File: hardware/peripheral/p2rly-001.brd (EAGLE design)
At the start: 18 x 31 mm, 4 parts, among them J4 RLY

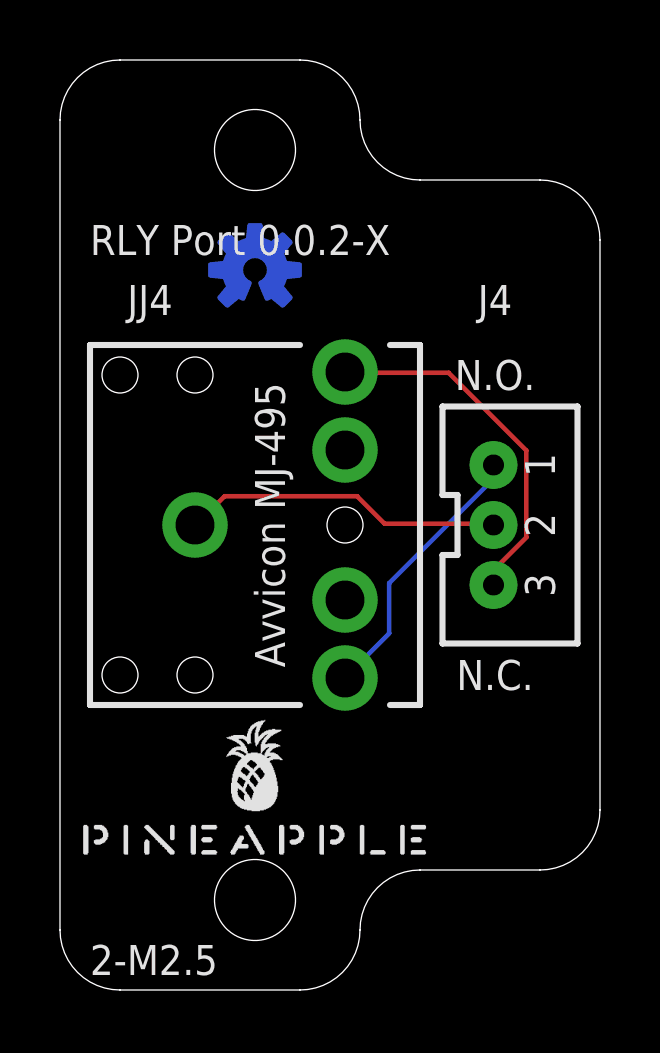
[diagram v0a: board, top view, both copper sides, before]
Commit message: Fixed polarity.
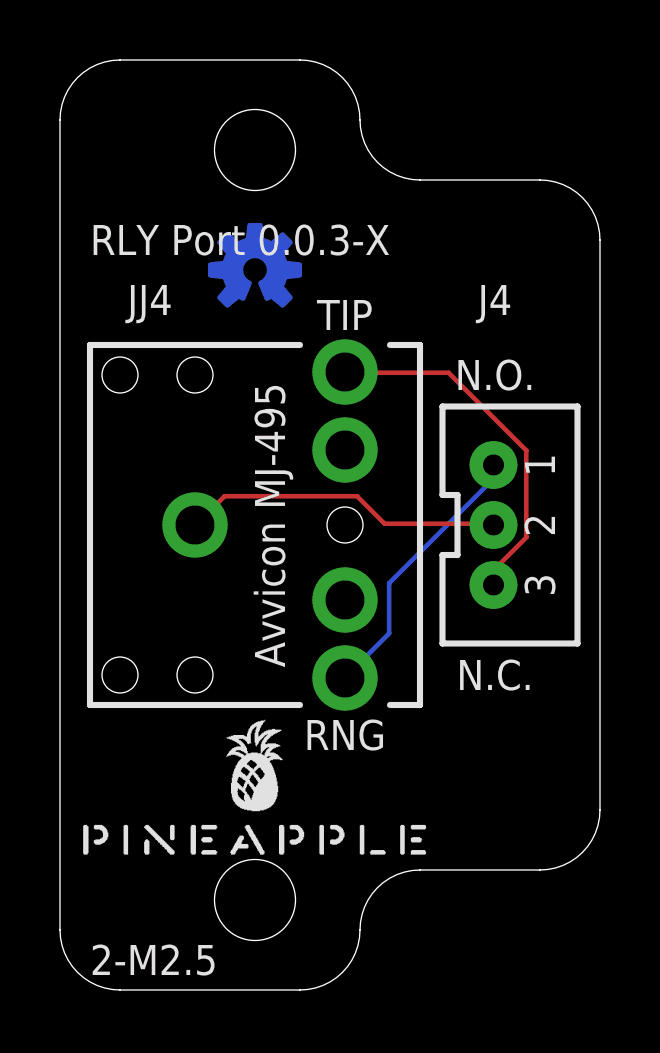
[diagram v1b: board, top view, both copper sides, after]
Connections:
- net NC: now also J4.1, JJ4.TIP; no longer J4.3, JJ4.RING
- net NO: now also J4.3, JJ4.RING; no longer J4.1, JJ4.TIP
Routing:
- net NO: track 9.15 -> 12.1 mm
- net NC: track 12.1 -> 9.15 mm
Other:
- board text added: "RLY Port 0.0.3-X"
- board text added: "RNG"
- board text added: "TIP"
- board text removed: "RLY Port 0.0.2-X"
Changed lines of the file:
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@@
 <grid distance="0.5" unitdist="mm" unit="mm" style="lines" multiple="2" display="yes" altdistance="5" altunitdist="mil" altunit="mil"/>
 <layers>
-<layer number="1" name="Top" color="4" fill="1" visible="no" active="yes"/>
-<layer number="16" name="Bottom" color="1" fill="1" visible="no" active="yes"/>
+<layer number="1" name="Top" color="4" fill="1" visible="yes" active="yes"/>
+<layer number="16" name="Bottom" color="1" fill="1" visible="yes" active="yes"/>
 <layer number="17" name="Pads" color="2" fill="1" visible="yes" active="yes"/>
 <layer number="18" name="Vias" color="2" fill="1" visible="yes" active="yes"/>
 <layer number="19" name="Unrouted" color="6" fill="1" visible="yes" active="yes"/>
 <layer number="20" name="Dimension" color="24" fill="1" visible="yes" active="yes"/>
-<layer number="21" name="tPlace" color="7" fill="1" visible="no" active="yes"/>
-<layer number="22" name="bPlace" color="7" fill="1" visible="yes" active="yes"/>
+<layer number="21" name="tPlace" color="7" fill="1" visible="yes" active="yes"/>
+<layer number="22" name="bPlace" color="7" fill="1" visible="no" active="yes"/>
 <layer number="23" name="tOrigins" color="15" fill="1" visible="yes" active="yes"/>
 <layer number="24" name="bOrigins" color="15" fill="1" visible="no" active="yes"/>
-<layer number="25" name="tNames" color="7" fill="1" visible="no" active="yes"/>
-<layer number="26" name="bNames" color="7" fill="1" visible="yes" active="yes"/>
+<layer number="25" name="tNames" color="7" fill="1" visible="yes" active="yes"/>
+<layer number="26" name="bNames" color="7" fill="1" visible="no" active="yes"/>
 <layer number="27" name="tValues" color="7" fill="1" visible="no" active="yes"/>
 <layer number="28" name="bValues" color="7" fill="1" visible="no" active="yes"/>
@@
 <rectangle x1="9" y1="0" x2="10" y2="5" layer="41"/>
 <rectangle x1="0" y1="0" x2="10" y2="1" layer="41"/>
-<text x="1" y="25" size="1" layer="25" align="center-left">RLY Port 0.0.2-X</text>
+<text x="1" y="25" size="1" layer="25" align="center-left">RLY Port 0.0.3-X</text>
 <text x="14.5" y="19" size="1" layer="26" rot="MR0" align="bottom-center">Tip</text>
 <text x="13" y="15.5" size="1" layer="26" rot="MR90" align="top-center">Sleeve</text>
@@
 <text x="16.5" y="17.5" size="1" layer="26" rot="MR90" align="center">1</text>
 <text x="16.5" y="13.5" size="1" layer="26" rot="MR90" align="center">3</text>
+<text x="9.5" y="22" size="1" layer="25" align="bottom-center">TIP</text>
+<text x="9.5" y="9" size="1" layer="25" align="top-center">RNG</text>
 </plain>
 <attributes>
@@
 </elements>
 <signals>
-<signal name="NO">
-<contactref element="JJ4" pad="TIP"/>
-<contactref element="J4" pad="1"/>
-<wire x1="14.3256" y1="16.9164" x2="14.3256" y2="17.3736" width="0.1524" layer="16"/>
-<wire x1="10.9728" y1="13.5636" x2="14.3256" y2="16.9164" width="0.1524" layer="16"/>
-<wire x1="10.9728" y1="11.8872" x2="10.9728" y2="13.5636" width="0.1524" layer="16"/>
-<wire x1="9.6012" y1="10.5156" x2="10.9728" y2="11.8872" width="0.1524" layer="16"/>
-<wire x1="14.3256" y1="17.3736" x2="14.45" y2="17.5" width="0.1524" layer="16"/>
-<wire x1="9.6012" y1="10.5156" x2="9.5" y2="10.4" width="0.1524" layer="16"/>
-</signal>
 <signal name="COMMON">
 <contactref element="JJ4" pad="SLEEVE"/>
@@
 </signal>
 <signal name="NC">
+<contactref element="JJ4" pad="TIP"/>
+<contactref element="J4" pad="1"/>
+<wire x1="14.3256" y1="16.9164" x2="14.3256" y2="17.3736" width="0.1524" layer="16"/>
+<wire x1="10.9728" y1="13.5636" x2="14.3256" y2="16.9164" width="0.1524" layer="16"/>
+<wire x1="10.9728" y1="11.8872" x2="10.9728" y2="13.5636" width="0.1524" layer="16"/>
+<wire x1="9.6012" y1="10.5156" x2="10.9728" y2="11.8872" width="0.1524" layer="16"/>
+<wire x1="14.3256" y1="17.3736" x2="14.45" y2="17.5" width="0.1524" layer="16"/>
+<wire x1="9.6012" y1="10.5156" x2="9.5" y2="10.4" width="0.1524" layer="16"/>
+</signal>
+<signal name="NO">
 <contactref element="JJ4" pad="RING"/>
 <contactref element="J4" pad="3"/>
